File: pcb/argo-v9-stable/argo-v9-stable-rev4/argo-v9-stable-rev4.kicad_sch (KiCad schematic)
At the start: 137 parts, among them IC2 MP2672GD-0000, J1 Sparkfun_NEO-N9M-SMA, J2 USB4125-GF-A, J3 LED_power_button_RGB_LED, J4 Conn_I2C_Molex_705450003, J5 Conn_I2C_Molex_705450003, K1 PRL3-5V-DC-1A, Q1 BSD840N, Q2 BSD840N, SW1 ON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

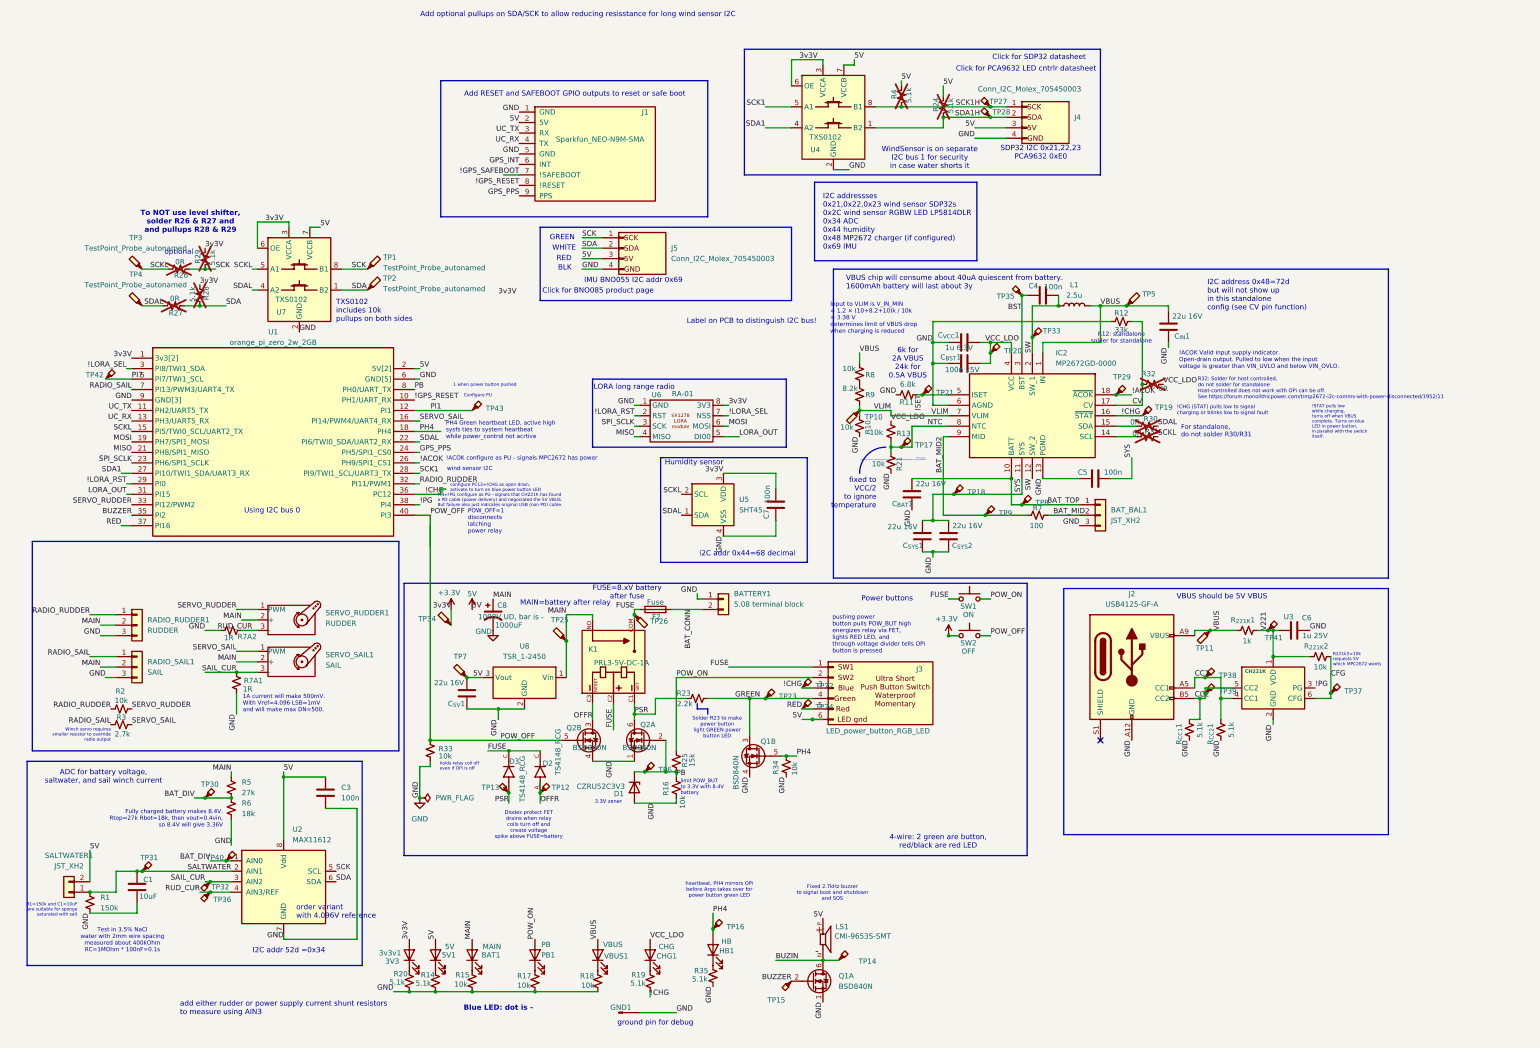
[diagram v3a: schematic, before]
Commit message: small edits to PCB rev 4 to note diode polarity and perhaps also missing pulldown on Buzzer
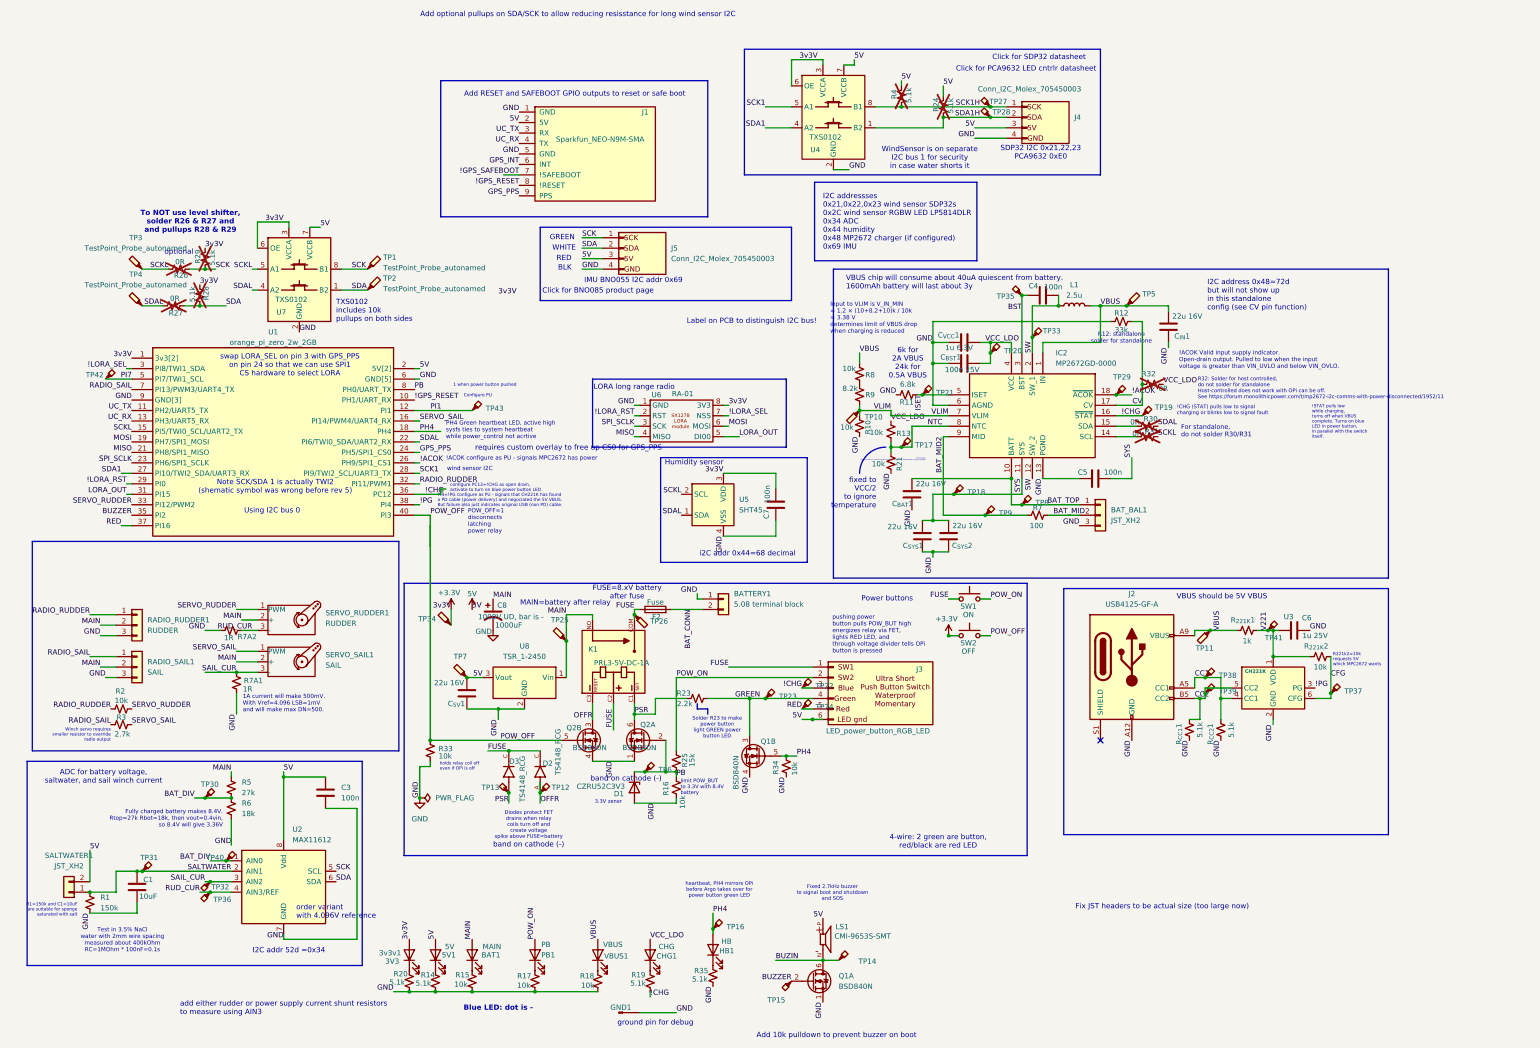
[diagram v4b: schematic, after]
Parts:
- U1: footprint Argo footprint Library:orange_pi_zero_2w_butted -> orangepi-zero:orange_pi_zero_2w
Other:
- note added: "Add 10k pulldown to prevent buzzer on boot"
- note added: "Fix JST headers to be actual size (too large now)"
- note added: "Note SCK/SDA 1 is actually TWI2 (shematic symbol was wrong before rev 5)"
- note added: "band on cathode (-)"
- note added: "requires custom overlay to free up CS0 for GPS_PPS"
- note added: "swap LORA_SEL on pin 3 with GPS_PPS on pin 24 so that we can use SPI1 CS hardware to select LORA"
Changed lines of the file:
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@@
 		)
 	)
+	(text "requires custom overlay to free up CS0 for GPS_PPS"
+		(exclude_from_sim no)
+		(at 201.168 123.444 0)
+		(effects
+			(font
+				(size 1.27 1.27)
+				(color 255 0 0 1)
+			)
+		)
+	)
 	(text "PI4=!PG configure as PU - signals that CH221K has found \na PD cable (power delivery) and negociated the 5V VBUS.\nBut failure also just indicates original USB (non PD) cable."
 		(exclude_from_sim no)
@@
 		)
 	)
+	(text "Note SCK/SDA 1 is actually TWI2\n(shematic symbol was wrong before rev 5)"
+		(exclude_from_sim no)
+		(at 130.048 132.842 0)
+		(effects
+			(font
+				(size 1.27 1.27)
+			)
+		)
+	)
 	(text "Fully charged battery makes 8.4V.\nRtop=27k Rbot=18k, then vout=0.4vin, \nso 8.4V will give 3.36V"
 		(exclude_from_sim no)
@@
 		)
 	)
+	(text "Fix JST headers to be actual size (too large now)"
+		(exclude_from_sim no)
+		(at 345.186 234.696 0)
+		(effects
+			(font
+				(size 1.27 1.27)
+				(color 255 0 0 1)
+			)
+		)
+	)
 	(text "IMU BNO055 I2C addr 0x69"
 		(exclude_from_sim no)
@@
 		)
 	)
+	(text "band on cathode (-)"
+		(exclude_from_sim no)
+		(at 215.138 203.708 0)
+		(effects
+			(font
+				(size 1.27 1.27)
+			)
+		)
+	)
+	(text "Add 10k pulldown to prevent buzzer on boot"
+		(exclude_from_sim no)
+		(at 266.192 265.938 0)
+		(effects
+			(font
+				(size 1.27 1.27)
+				(color 255 0 0 1)
+			)
+		)
+	)
 	(text "Power buttons"
 		(exclude_from_sim no)
@@
 		)
 	)
+	(text "band on cathode (-)"
+		(exclude_from_sim no)
+		(at 191.516 219.71 0)
+		(effects
+			(font
+				(size 1.27 1.27)
+			)
+		)
+	)
 	(text "WindSensor is on separate \nI2C bus 1 for security \nin case water shorts it"
 		(exclude_from_sim no)
@@
 		)
 	)
+	(text "swap LORA_SEL on pin 3 with GPS_PPS\non pin 24 so that we can use SPI1 \nCS hardware to select LORA"
+		(exclude_from_sim no)
+		(at 133.604 103.378 0)
+		(effects
+			(font
+				(size 1.27 1.27)
+				(color 255 0 0 1)
+			)
+		)
+	)
 	(text "4-wire: 2 green are button,\nred/black are red LED"
 		(exclude_from_sim no)
@@
 	)
 	(label "PI7"
-		(at 95.25 106.68 0)
+		(at 95.25 106.68 180)
 		(effects
 			(font
 				(size 1.27 1.27)
 			)
-			(justify left bottom)
+			(justify right bottom)
 		)
 	)
@@
 			)
 		)
-		(property "Footprint" "Argo footprint Library:orange_pi_zero_2w_butted"
+		(property "Footprint" "orangepi-zero:orange_pi_zero_2w"
 			(at 100.33 100.33 0)
 			(effects

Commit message: pcb and glands
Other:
- note added: "IMU BNO085 I2C addr 0x69"
- note removed: "IMU BNO055 I2C addr 0x69"
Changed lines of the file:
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@@
 		)
 	)
-	(text "IMU BNO055 I2C addr 0x69"
+	(text "IMU BNO085 I2C addr 0x69"
 		(exclude_from_sim no)
 		(at 216.916 82.804 0)

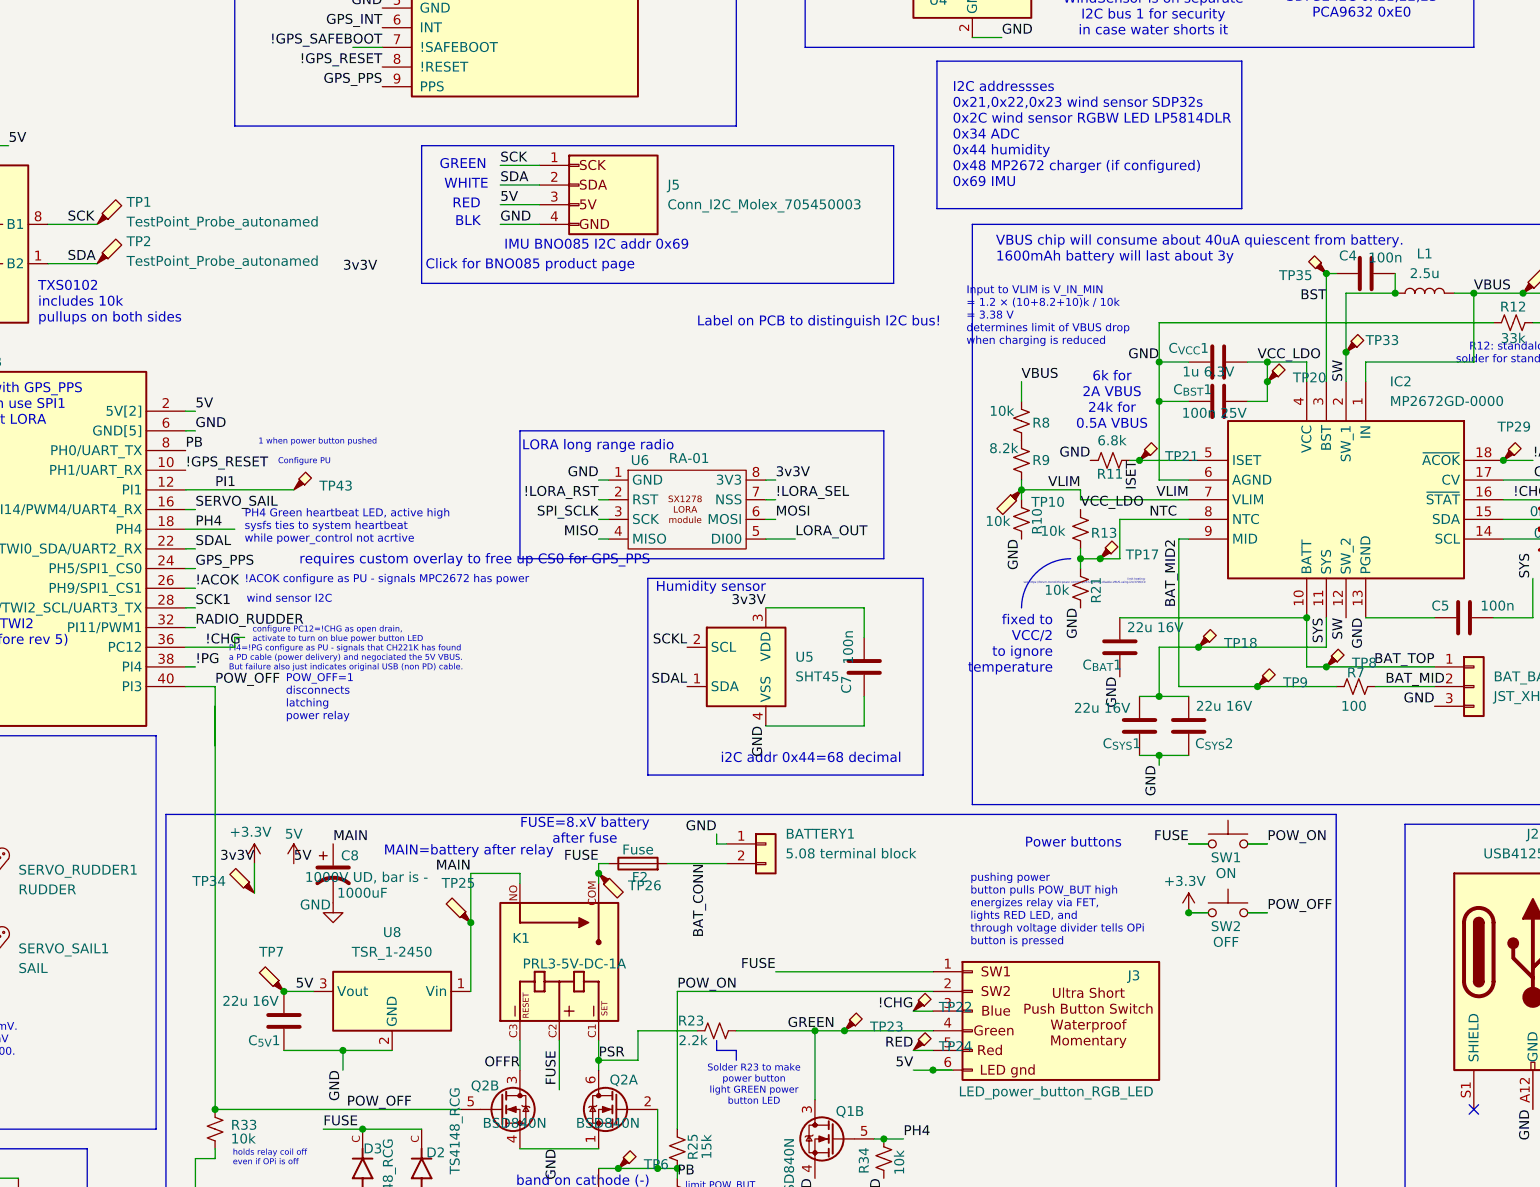
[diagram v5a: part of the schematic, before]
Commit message: latest v5 schematics and 3d design upated including hose coupleeer for pressure test
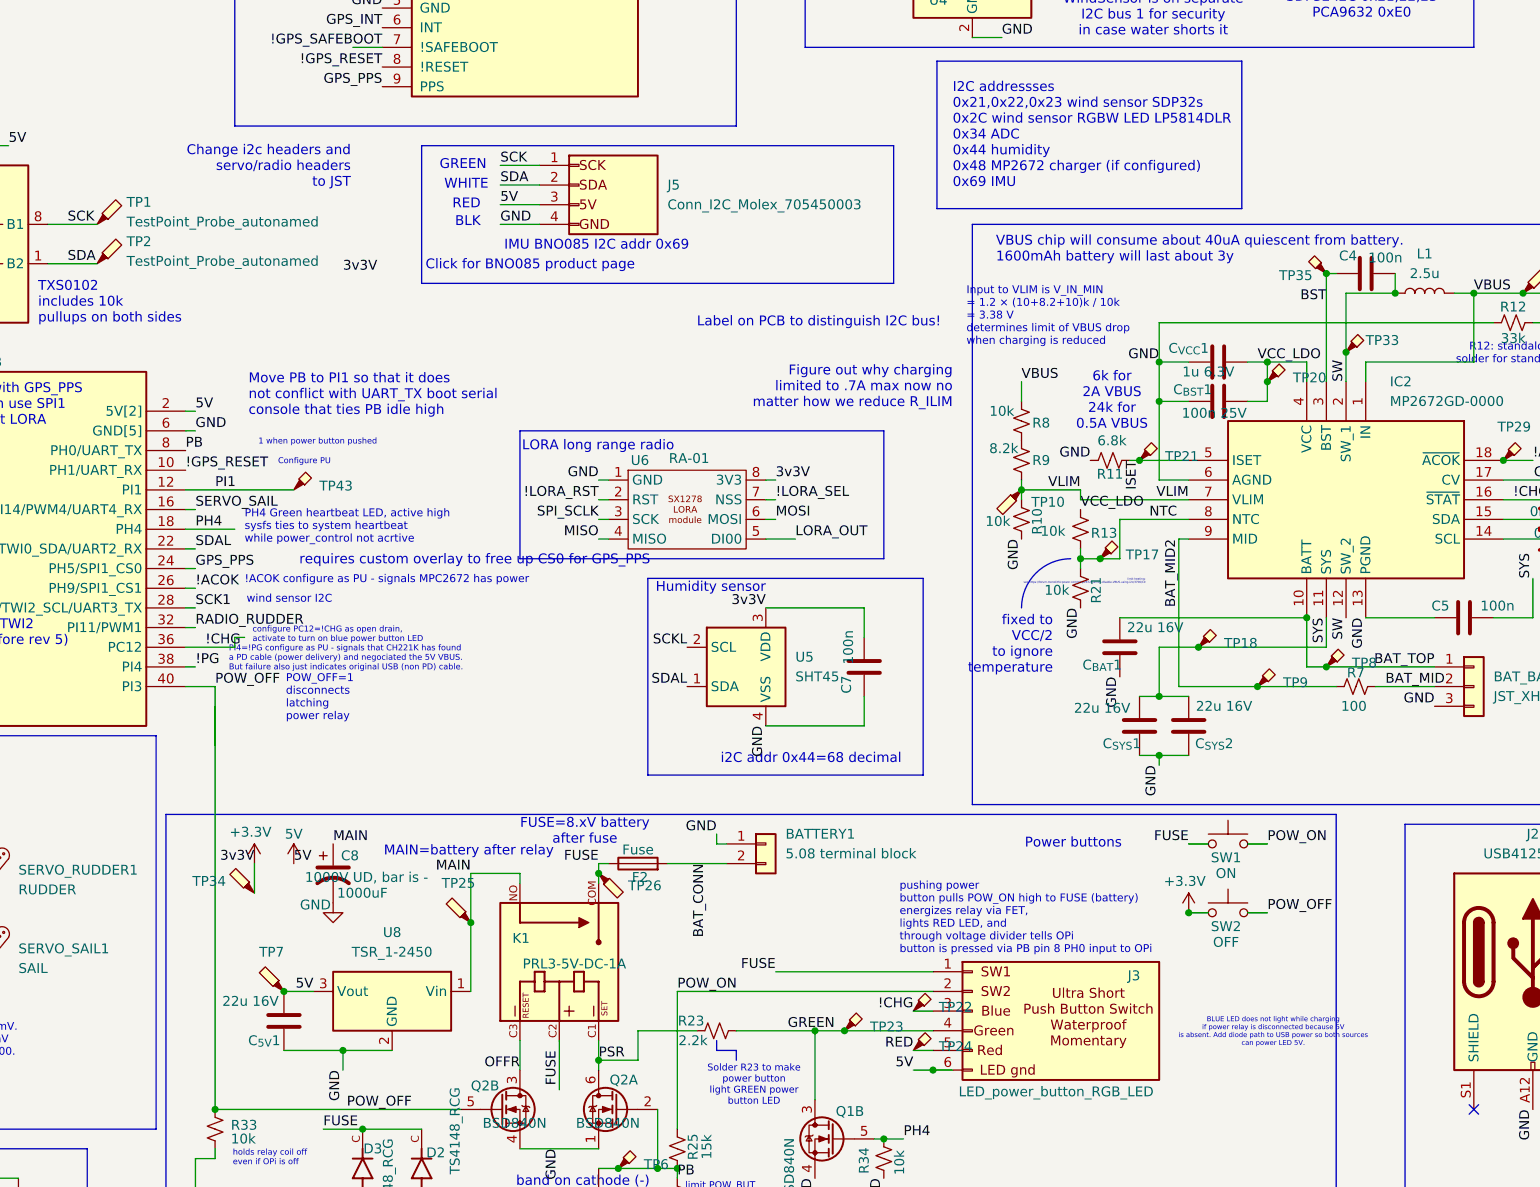
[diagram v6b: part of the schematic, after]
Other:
- note added: "BLUE LED does not light while charging if power relay is disconnected because 5V is absent. Add diode path to USB power so both sources can power LED 5V."
- note added: "Change i2c headers and servo/radio headers to JST"
- note added: "Figure out why charging limited to .7A max now no matter how we reduce R_ILIM"
- note added: "Move PB to PI1 so that it does not conflict with UART_TX boot serial console that ties PB idle high"
- note added: "pushing power button pulls POW_ON high to FUSE (battery) energizes relay via FET, lights RED LED, and through voltage divider tells OPi button is pressed via PB pin 8 PH0 input to OPi"
- note removed: "pushing power button pulls POW_BUT high energizes relay via FET, lights RED LED, and through voltage divider tells OPi button is pressed"
